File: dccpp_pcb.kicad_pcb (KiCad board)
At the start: 2 copper layers, 101.6 x 63.5 mm, 64 parts, among them J1 USB_B_Micro, J10 OSTTC022162, J11 OSTTC022162, J12 OSTTC022162, J2 AVR-ISP-6, J3 OSTTC022162, J4 OSTTC022162, J5 OSTTC022162, J6 OSTTC022162, J7 OSTTC022162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

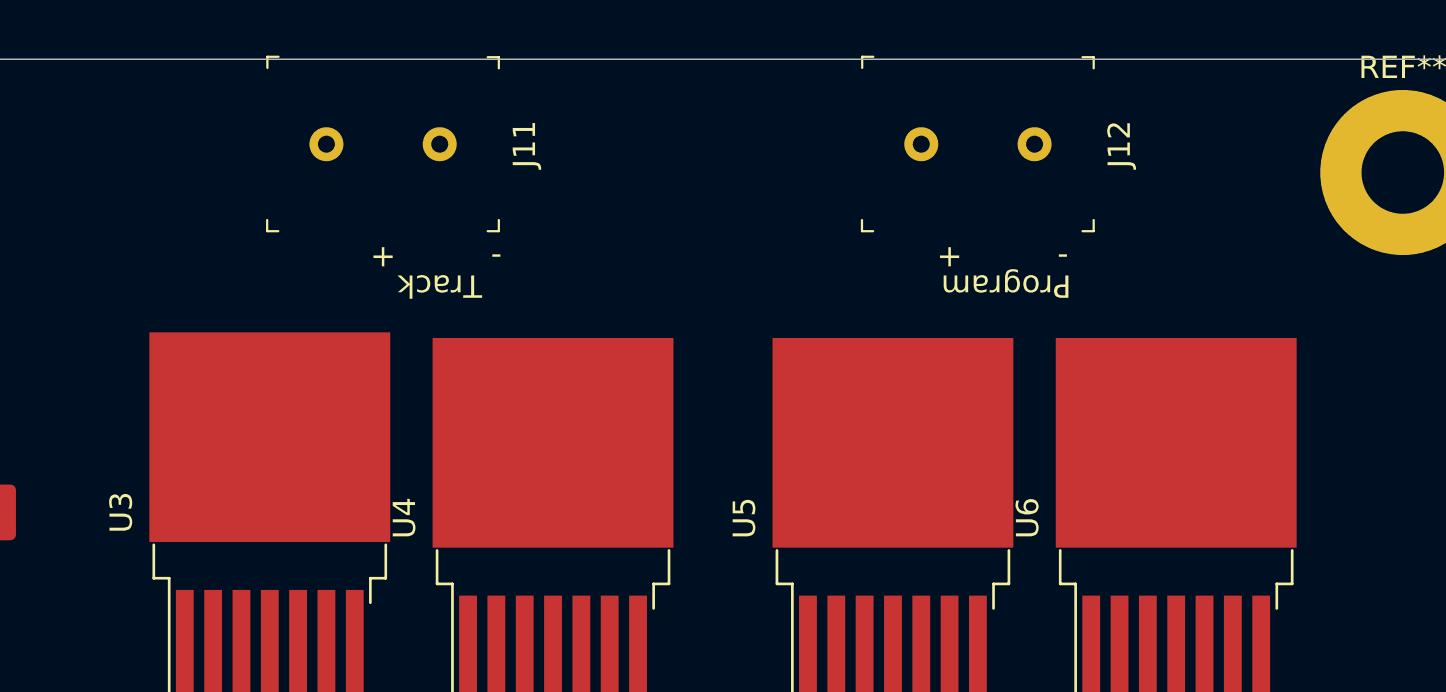
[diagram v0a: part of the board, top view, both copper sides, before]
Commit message: Setup design rules
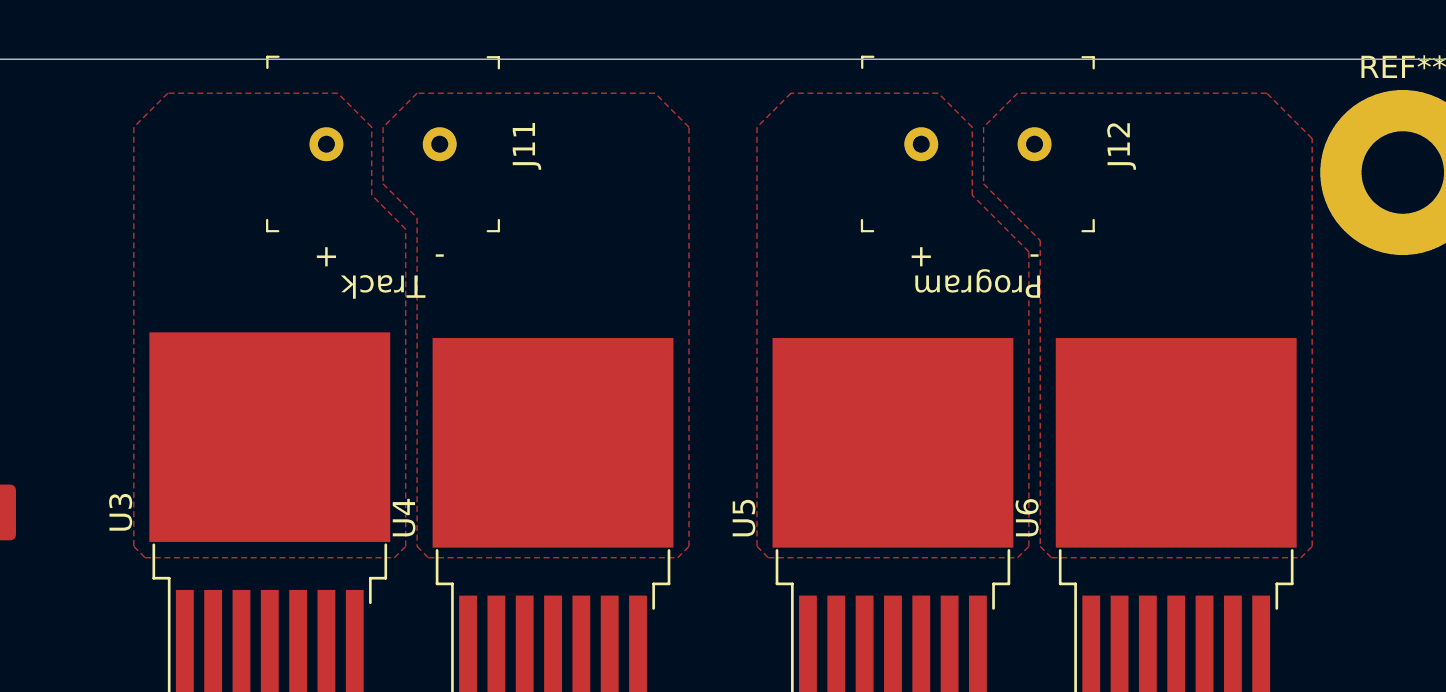
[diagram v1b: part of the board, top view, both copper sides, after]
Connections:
- net Net-(J11-Pad1) renamed /TRACK_N
- net Net-(J11-Pad2) renamed /TRACK_P
- net Net-(J12-Pad1) renamed /PROG_N
- net Net-(J12-Pad2) renamed /PROG_P
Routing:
- added copper zone on F.Cu, net /PROG_N
- added copper zone on F.Cu, net /PROG_P
- added copper zone on F.Cu, net /TRACK_N
- added copper zone on F.Cu, net /TRACK_P
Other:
- net class Default: clearance 0.2 -> 0.1524; trace_width 0.25 -> 0.1524; via_dia 0.8 -> 0.508; via_drill 0.4 -> 0.254
- net class Power added: clearance 0.1524, trace_width 5.08, via_dia 0.508, via_drill 0.254
- rule pad_to_mask_clearance: 0.051 -> 0.0508
- rule solder_mask_min_width: 0.25 -> 0.254
- rule trace_clearance: 0.2 -> 0.1524
- rule trace_min: 0.2 -> 0.1524
- rule via_min_drill: 0.3 -> 0.254
- rule via_min_size: 0.4 -> 0.508

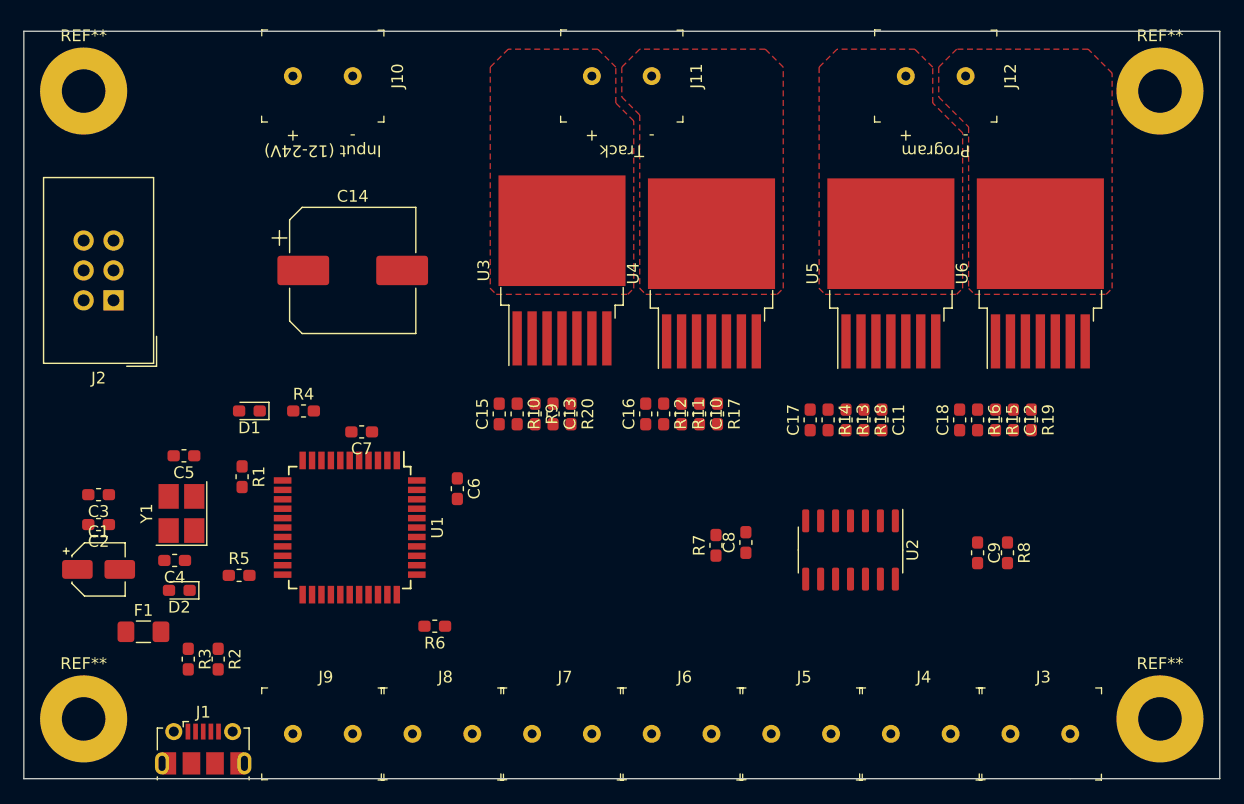
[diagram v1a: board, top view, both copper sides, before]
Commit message: Cleanup of h-bridge layout
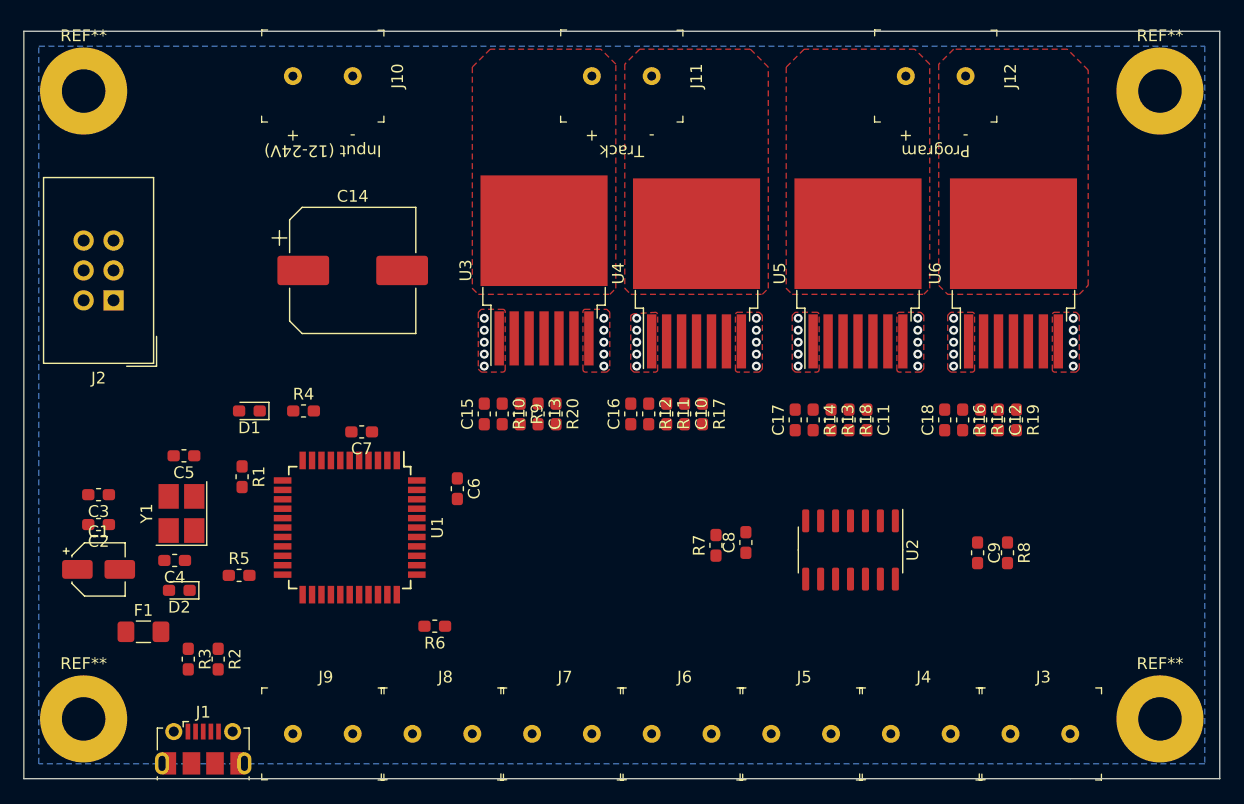
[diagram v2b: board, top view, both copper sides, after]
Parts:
- moved U5 2.79 mm to (134.4, 109.5)
- moved U6 2.29 mm to (147.6, 109.5)
- moved U3 1.52 mm to (107.7, 109.2)
- moved C11 1.27 mm to (135.1, 121.9)
- moved C12 1.27 mm to (146.3, 121.9)
- moved C18 1.27 mm to (141.7, 121.9)
- moved R15 1.27 mm to (144.8, 121.9)
- moved R16 1.27 mm to (143.3, 121.9)
- moved R19 1.27 mm to (147.8, 121.9)
- moved C10 1.27 mm to (119.6, 121.4)
- moved C13 1.27 mm to (107.2, 121.4)
- moved C15 1.27 mm to (102.6, 121.4)
- moved C16 1.27 mm to (115.1, 121.4)
- moved R10 1.27 mm to (104.1, 121.4)
- moved R11 1.27 mm to (118.1, 121.4)
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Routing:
- net VCC: vias 0 -> 20
- net GND: vias 0 -> 20
- added copper zone on B.Cu, net GND
- added copper zone on F.Cu, net GND
- added copper zone on F.Cu, net VCC

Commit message: More layout work
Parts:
- moved C8 15.0 mm to (112.8, 123.4)
- moved R7 14.3 mm to (111.3, 123.4)
- moved R8 12.2 mm to (139.2, 124.0), turned to 90 degrees
- moved C9 11.5 mm to (137.7, 124.0), turned to 90 degrees
- moved C14 3.70 mm to (90.4, 105.7)
- moved U1 0.76 mm to (91.9, 131.1), turned to 0 degrees
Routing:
- net /PROG_SENSE: track 0.00 -> 67.2 mm, vias 0 -> 3
- net VCC: vias 20 -> 36
- added copper zone on B.Cu, net VCC

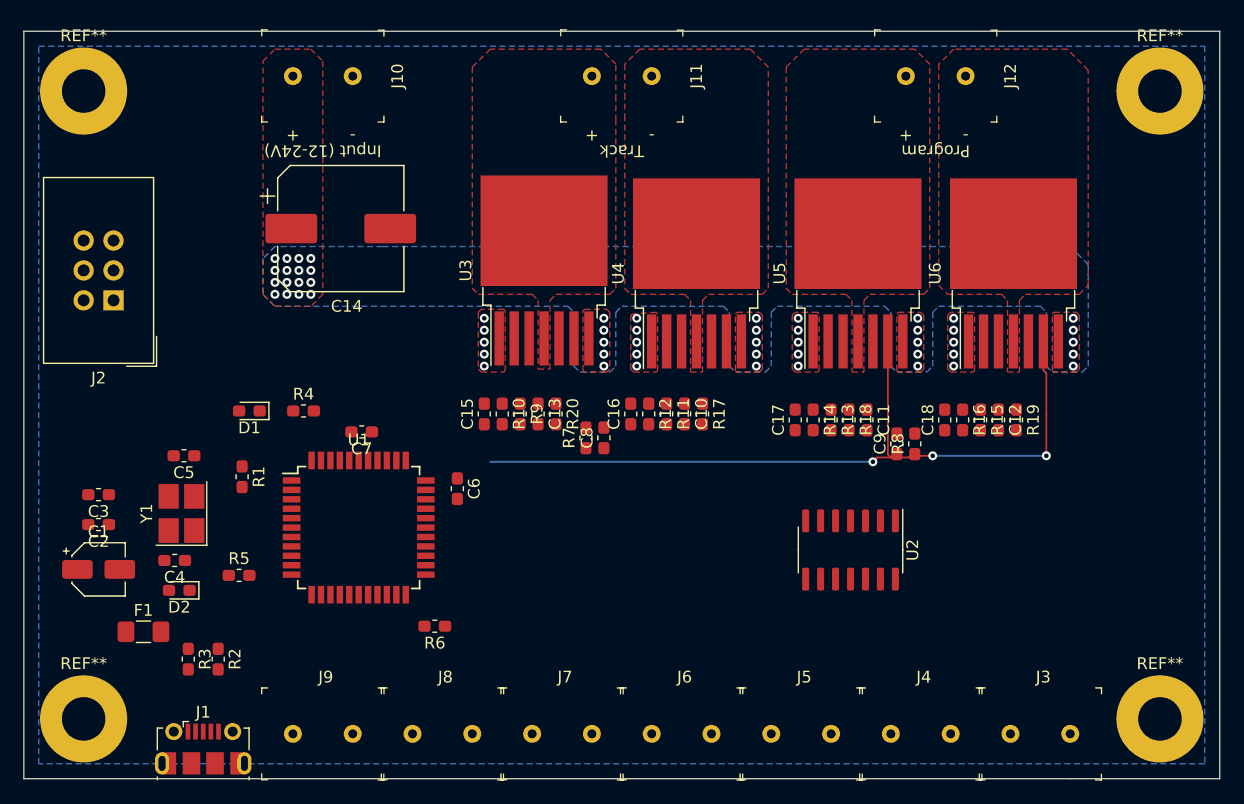
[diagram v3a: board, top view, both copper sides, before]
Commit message: Start work on signal layout.
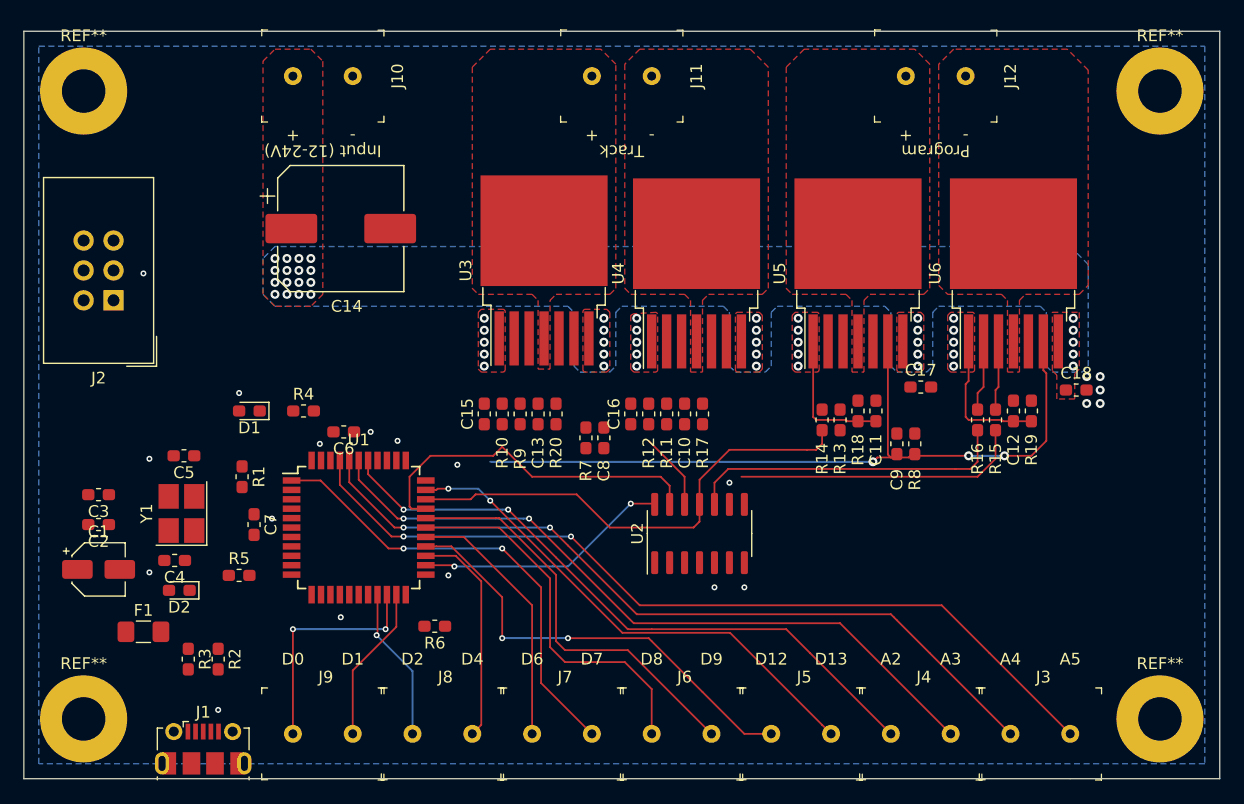
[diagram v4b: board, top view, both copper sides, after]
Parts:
- moved U2 12.9 mm to (120.9, 131.6), turned to 90 degrees
- moved C7 12.1 mm to (83.1, 130.8), turned to 270 degrees
- moved C18 11.5 mm to (152.9, 119.4), turned to 0 degrees
- moved C17 11.0 mm to (139.7, 119.1), turned to 0 degrees
- moved C6 10.8 mm to (90.7, 122.9), turned to 180 degrees
- moved C12 1.48 mm to (147.6, 121.2)
- moved R19 1.48 mm to (149.1, 121.2)
- moved R15 1.27 mm to (146.1, 121.9)
- moved R16 1.27 mm to (144.5, 121.9)
- moved C11 1.08 mm to (135.9, 121.2)
- moved R18 1.08 mm to (134.4, 121.2)
- moved R13 0.76 mm to (132.8, 121.9)
- moved R14 0.76 mm to (131.3, 121.9)
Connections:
- U2 pad 1: /OUT -> GND
- U2 pad 10: Net-(U2-Pad10) -> Net-(R16-Pad2)
- U2 pad 11: GND -> /PROG
- U2 pad 12: Net-(U2-Pad12) -> Net-(R12-Pad2)
- U2 pad 13: GND -> /OUT
- U2 pad 2: Net-(R12-Pad2) -> Net-(U2-Pad2)
- U2 pad 3: /PROG -> GND
- U2 pad 4: Net-(R16-Pad2) -> Net-(U2-Pad4)
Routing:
- net /A5: track 0.00 -> 72.9 mm, vias 0 -> 2
- net /A4: track 0.00 -> 66.9 mm, vias 0 -> 2
- net /A3: track 0.00 -> 60.9 mm, vias 0 -> 2
- net /A2: track 0.00 -> 54.7 mm, vias 0 -> 2
- net /D13: track 0.00 -> 43.1 mm, vias 0 -> 2
- net /PROG: track 0.00 -> 41.2 mm
- net /D7: track 0.00 -> 39.2 mm, vias 0 -> 2
- net /D12: track 0.00 -> 38.0 mm, vias 0 -> 2
- net /D9: track 0.00 -> 35.2 mm
- net /D8: track 0.00 -> 32.1 mm
- net /OUT: track 0.00 -> 30.1 mm
- net Net-(R16-Pad2): track 0.00 -> 27.6 mm
- net /PROG_EN: track 0.00 -> 24.6 mm
- net GND: track 0.00 -> 24.2 mm, vias 20 -> 40
- net /D6: track 0.00 -> 22.4 mm
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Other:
- board text added: "A2"
- board text added: "A3"
- board text added: "A4"
- board text added: "A5"
- board text added: "D0"
- board text added: "D1"
- board text added: "D12"
- board text added: "D13"
- board text added: "D2"
- board text added: "D4"
- board text added: "D6"
- board text added: "D7"
- board text added: "D8"
- board text added: "D9"

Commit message: More routing.
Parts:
- moved C9 3.14 mm to (140.7, 124.7)
- moved R8 3.14 mm to (142.2, 124.7)
- moved C17 1.37 mm to (138.9, 120.3), turned to 270 degrees
- moved C18 1.17 mm to (152.1, 120.3), turned to 270 degrees
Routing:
- net Net-(R16-Pad2): track 27.6 -> 6.18 mm
- net Net-(C12-Pad1): track 0.00 -> 6.66 mm
- net (no net): vias 0 -> 5
- added copper zone on F.Cu, net (none)

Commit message: More routing
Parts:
- added C19: 0.1uF 10V, Capacitor_SMD:C_0603_1608Metric_Pad1.05x0.95mm_HandSolder, F.Cu at (82.8, 117.9)
- added C20: 0.1uF 10V, Capacitor_SMD:C_0603_1608Metric_Pad1.05x0.95mm_HandSolder, F.Cu at (83.3, 135.6)
- added C21: 0.1uF 10V, Capacitor_SMD:C_0603_1608Metric_Pad1.05x0.95mm_HandSolder, F.Cu at (95.5, 132.1)
- added C22: 0.1uF 10V, Capacitor_SMD:C_0603_1608Metric_Pad1.05x0.95mm_HandSolder, F.Cu at (91.4, 119.4)
- added C23: 0.1uF 10V, Capacitor_SMD:C_0603_1608Metric_Pad1.05x0.95mm_HandSolder, F.Cu at (77.7, 122.9)
- added C24: 0.1uF 10V, Capacitor_SMD:C_0603_1608Metric_Pad1.05x0.95mm_HandSolder, F.Cu at (115.3, 133.1)
- moved D2 21.4 mm to (98.0, 135.1), turned to 0 degrees
- moved R6 18.3 mm to (95.5, 121.4)
- moved C5 15.8 mm to (82.8, 139.7), turned to 270 degrees
- moved C4 14.8 mm to (89.9, 139.7), turned to 270 degrees
- moved Y1 13.7 mm to (86.4, 139.7), turned to 180 degrees
- moved R4 13.0 mm to (76.2, 128.0), turned to 270 degrees
- moved R5 12.7 mm to (94.5, 135.1), turned to 180 degrees
- moved D1 10.5 mm to (74.7, 128.0), turned to 270 degrees
- moved C16 10.5 mm to (125.5, 120.3), turned to 270 degrees
- moved C15 9.22 mm to (111.8, 120.3), turned to 270 degrees
- moved R1 9.18 mm to (79.8, 135.6), turned to 180 degrees
- moved C6 7.74 mm to (84.8, 117.9), turned to 270 degrees
- moved U1 6.20 mm to (86.9, 127.5)
- moved C7 6.02 mm to (77.7, 128.0)
- moved R7 3.56 mm to (114.8, 123.4)
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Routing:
- net GND: track 24.2 -> 91.6 mm, vias 40 -> 61
- net /RESET: track 0.00 -> 39.5 mm, vias 0 -> 2
- net /OUT_SENSE: track 0.00 -> 34.0 mm
- net Net-(R3-Pad1): track 0.00 -> 30.0 mm
- net Net-(R2-Pad1): track 0.00 -> 25.5 mm
- net +5V: track 21.7 -> 31.5 mm
- net Net-(C5-Pad1): track 0.00 -> 8.19 mm
- net Net-(C4-Pad1): track 0.00 -> 8.01 mm
- net Net-(C13-Pad1): track 0.00 -> 7.17 mm
- net Net-(C10-Pad1): track 0.00 -> 7.08 mm
- net Net-(R10-Pad1): track 0.00 -> 6.85 mm
- net Net-(R9-Pad1): track 0.00 -> 6.75 mm
- net Net-(C11-Pad1): track 0.00 -> 6.66 mm
- net Net-(R11-Pad1): track 0.00 -> 6.23 mm
- net Net-(R12-Pad1): track 0.00 -> 6.23 mm
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- removed copper zone on F.Cu, net (none)

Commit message: More layout
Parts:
- moved C3 5.84 mm to (69.8, 134.1), turned to 0 degrees
- moved C2 4.83 mm to (69.8, 135.6), turned to 0 degrees
- moved C1 4.64 mm to (70.6, 139.2), turned to 180 degrees
- moved R1 2.11 mm to (78.6, 133.9), turned to 270 degrees
- moved R2 1.02 mm to (79.2, 142.2)
- moved R3 1.02 mm to (77.7, 142.2)
- moved C9 0.99 mm to (141.5, 124.1)
- moved R8 0.99 mm to (143.0, 124.1)
- moved C7 0.89 mm to (78.6, 128.0)
- moved F1 0.72 mm to (74.7, 142.7)
- moved C20 0.38 mm to (83.3, 136.0), turned to 0 degrees
- moved C21 0.38 mm to (95.9, 132.1)
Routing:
- net +5V: track 31.5 -> 76.9 mm
- net /MOSI: track 0.00 -> 34.7 mm, vias 0 -> 2
- net /SCK: track 0.00 -> 31.8 mm, vias 0 -> 2
- net /MISO: track 0.00 -> 30.3 mm, vias 0 -> 2
- net /A5: track 72.9 -> 54.4 mm, vias 2 -> 0
- net /A4: track 66.9 -> 49.9 mm, vias 2 -> 0
- net /A3: track 60.9 -> 45.5 mm, vias 2 -> 0
- net GND: track 91.6 -> 106.3 mm, vias 61 -> 65
- net /D7: track 39.2 -> 24.8 mm, vias 2 -> 0
- net /A2: track 54.7 -> 41.0 mm, vias 2 -> 0
- net Net-(R16-Pad2): track 6.18 -> 15.0 mm
- net /D8: track 32.1 -> 24.4 mm
- net /D2: track 13.1 -> 20.6 mm, vias 1 -> 2
- net /D9: track 35.2 -> 27.7 mm
- net /D13: track 43.1 -> 36.6 mm, vias 2 -> 0
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
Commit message: Routing almost complete
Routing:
- net /OUT_EN: track 0.00 -> 42.7 mm, vias 0 -> 5
- net /A5: track 54.4 -> 88.4 mm
- net /A4: track 49.9 -> 82.2 mm
- net /A3: track 45.5 -> 76.1 mm
- net /A2: track 41.0 -> 69.9 mm
- net /OUT_SENSE: track 34.0 -> 59.9 mm, vias 0 -> 4
- net /PROG_SENSE: track 64.6 -> 89.2 mm, vias 3 -> 6
- net /PROG_EN: track 24.6 -> 46.9 mm, vias 0 -> 3
- net GND: track 106.3 -> 127.5 mm, vias 65 -> 67
- net /D7: track 24.8 -> 44.6 mm, vias 0 -> 2
- net +5V: track 76.9 -> 96.1 mm, vias 2 -> 3
- net Net-(R16-Pad2): track 15.0 -> 28.2 mm
- net /D13: track 36.6 -> 49.6 mm
- net /D9: track 27.7 -> 38.7 mm
- net /D12: track 32.1 -> 42.5 mm, vias 0 -> 2
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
